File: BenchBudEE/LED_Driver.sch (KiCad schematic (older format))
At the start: 6 parts, among them U5 AP5726

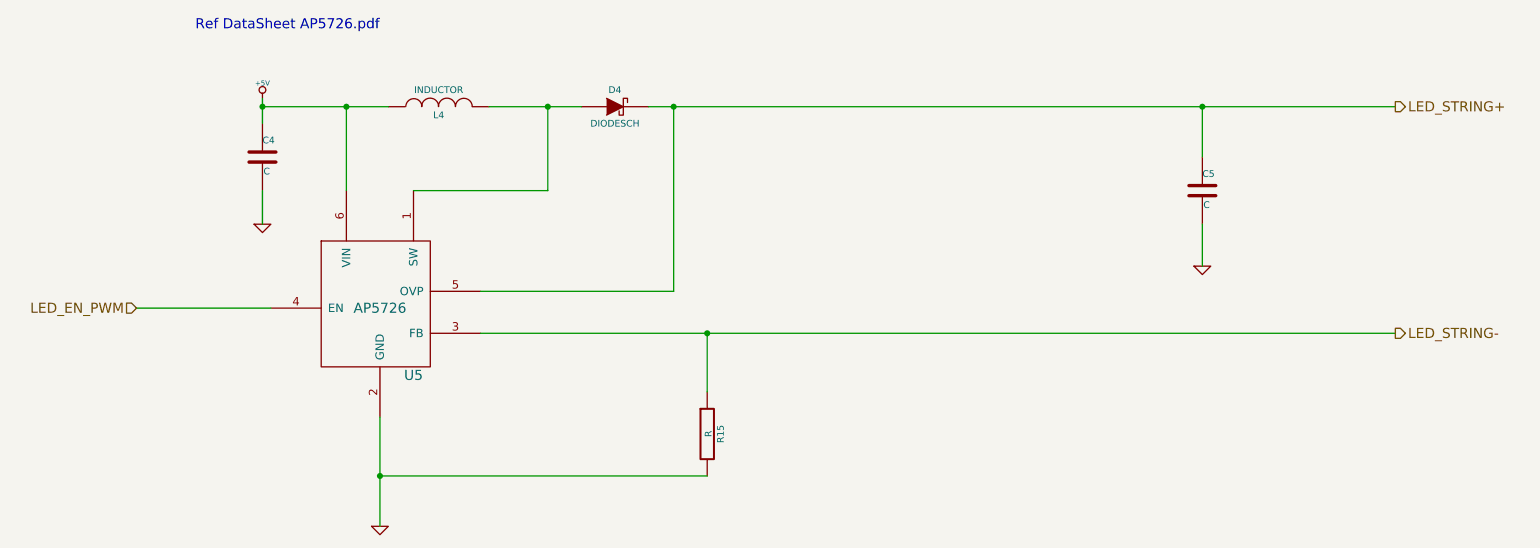
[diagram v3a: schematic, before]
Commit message: Associated the LED Driver module components.
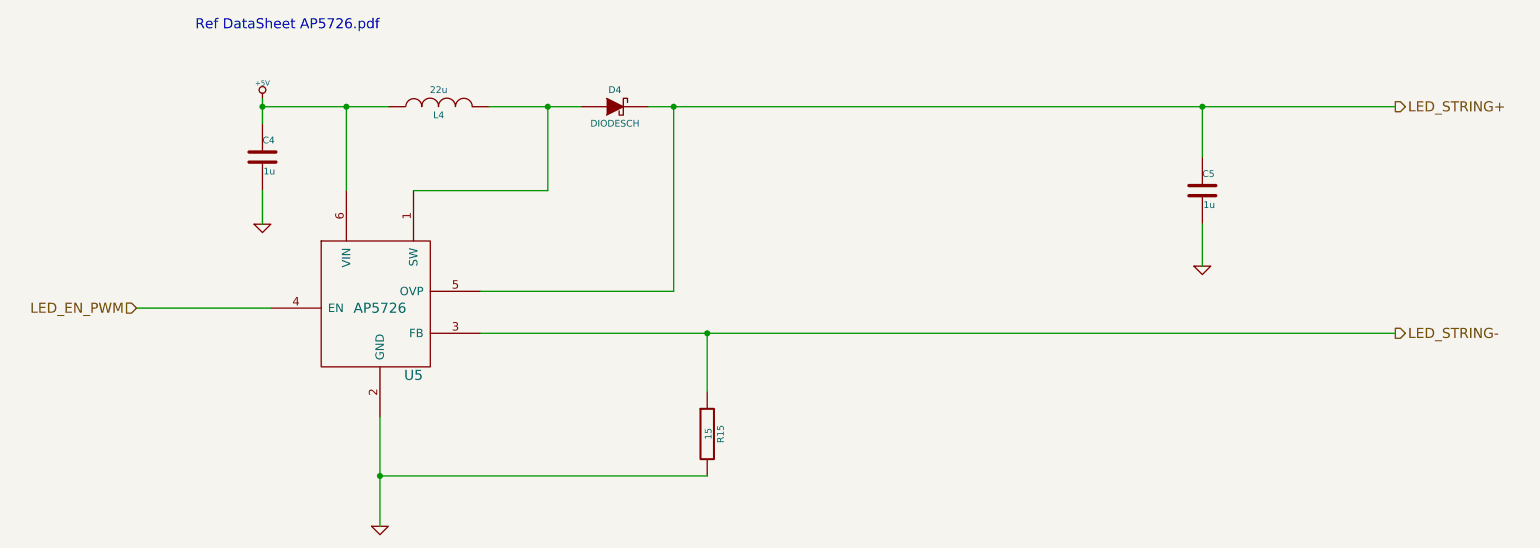
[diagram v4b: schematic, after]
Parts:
- C4, C5: value C -> 1u
- L4: value INDUCTOR -> 22u; MFG Name (none) -> Taiyo Yuden; MFG Part Number (none) -> NR4012T220M
- R15: value R -> 15
- U5: MFG Name (none) -> Diodes Inc; MFG Part Number (none) -> AP5726WG-7
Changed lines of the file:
@@
 Sheet 5 9
 Title ""
-Date "23 feb 2014"
+Date "24 feb 2014"
 Rev ""
 Comp ""
@@
 F 2 "" H 3050 2300 60  0000 C CNN
 F 3 "" H 3050 2300 60  0000 C CNN
+F 4 "Diodes Inc" H 3050 2300 60  0001 C CNN "MFG Name"
+F 5 "AP5726WG-7" H 3050 2300 60  0001 C CNN "MFG Part Number"
 	1    3050 2300
 	1    0    0    -1
@@
 P 2350 1400
 F 0 "C4" H 2350 1500 40  0000 L CNN
-F 1 "C" H 2356 1315 40  0000 L CNN
+F 1 "1u" H 2356 1315 40  0000 L CNN
 F 2 "~" H 2388 1250 30  0000 C CNN
 F 3 "~" H 2350 1400 60  0000 C CNN
@@
 P 7950 1600
 F 0 "C5" H 7950 1700 40  0000 L CNN
-F 1 "C" H 7956 1515 40  0000 L CNN
+F 1 "1u" H 7956 1515 40  0000 L CNN
 F 2 "~" H 7988 1450 30  0000 C CNN
 F 3 "~" H 7950 1600 60  0000 C CNN
@@
 P 3400 1100
 F 0 "L4" V 3350 1100 40  0000 C CNN
-F 1 "INDUCTOR" V 3500 1100 40  0000 C CNN
+F 1 "22u" V 3500 1100 40  0000 C CNN
 F 2 "~" H 3400 1100 60  0000 C CNN
 F 3 "~" H 3400 1100 60  0000 C CNN
+F 4 "Taiyo Yuden" H 3400 1100 60  0001 C CNN "MFG Name"
+F 5 "NR4012T220M" H 3400 1100 60  0001 C CNN "MFG Part Number"
 	1    3400 1100
 	0    -1   -1   0
@@
 P 5000 3050
 F 0 "R15" V 5080 3050 40  0000 C CNN
-F 1 "R" V 5007 3051 40  0000 C CNN
+F 1 "15" V 5007 3051 40  0000 C CNN
 F 2 "~" V 4930 3050 30  0000 C CNN
 F 3 "~" H 5000 3050 30  0000 C CNN

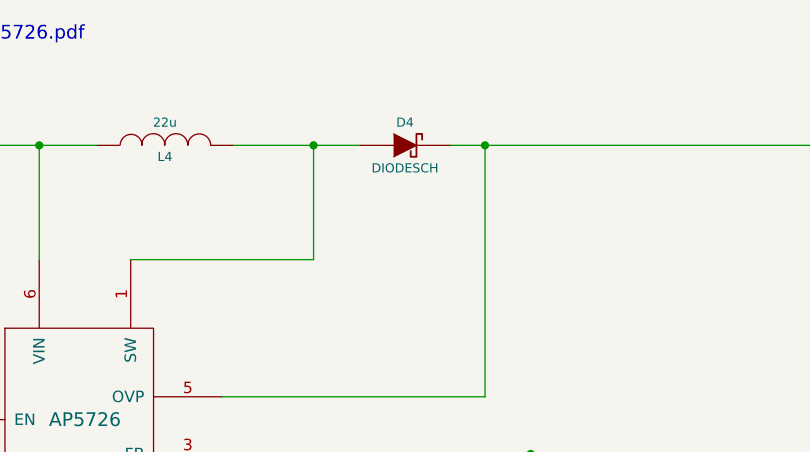
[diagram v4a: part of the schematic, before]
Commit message: Roughly placed the LED Driver module components.
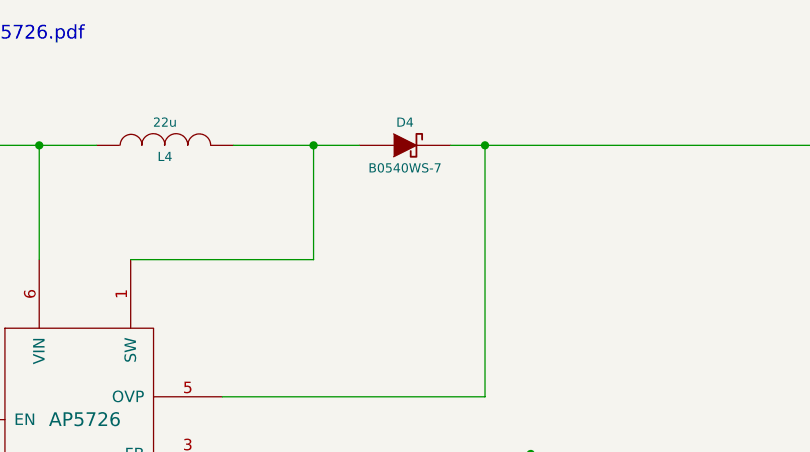
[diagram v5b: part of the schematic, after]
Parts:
- D4: value DIODESCH -> B0540WS-7; MFG Part Number (none) -> B0540WS-7
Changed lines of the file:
@@
 P 4450 1100
 F 0 "D4" H 4450 1200 40  0000 C CNN
-F 1 "DIODESCH" H 4450 1000 40  0000 C CNN
+F 1 "B0540WS-7" H 4450 1000 40  0000 C CNN
 F 2 "~" H 4450 1100 60  0000 C CNN
 F 3 "~" H 4450 1100 60  0000 C CNN
+F 4 "B0540WS-7" H 4450 1100 60  0001 C CNN "MFG Part Number"
 	1    4450 1100
 	1    0    0    -1
